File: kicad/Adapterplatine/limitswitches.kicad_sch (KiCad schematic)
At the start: 15 parts, among them X12 Conn_01x05_Pin, X13 Conn_01x05_Pin, X15 Conn_01x05_Pin, X16 Conn_01x05_Pin, X37 Conn_01x02_Pin, X39 Conn_01x02_Pin

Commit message: Leitungsverlegung Adapterplatine abgeschlossen
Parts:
- EndStopX1: Hersteller (none) -> Test
- R1, R2, R3: footprint Resistor_THT:R_Axial_DIN0207_L6.3mm_D2.5mm_P2.54mm_Vertical -> Resistor_THT:R_Axial_DIN0207_L6.3mm_D2.5mm_P10.16mm_Horizontal
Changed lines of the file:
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@@
 			)
 		)
-		(property "Footprint" "Resistor_THT:R_Axial_DIN0207_L6.3mm_D2.5mm_P2.54mm_Vertical"
+		(property "Footprint" "Resistor_THT:R_Axial_DIN0207_L6.3mm_D2.5mm_P10.16mm_Horizontal"
 			(at 46.482 73.66 90)
 			(hide yes)
@@
 		)
 		(property "Description" "Resistor"
+			(at 48.26 73.66 0)
+			(hide yes)
+			(show_name no)
+			(do_not_autoplace no)
+			(effects
+				(font
+					(size 1.27 1.27)
+				)
+			)
+		)
+		(property "Hersteller" ""
+			(at 48.26 73.66 0)
+			(hide yes)
+			(show_name no)
+			(do_not_autoplace no)
+			(effects
+				(font
+					(size 1.27 1.27)
+				)
+			)
+		)
+		(property "Herstellerbezeichnung" ""
+			(at 48.26 73.66 0)
+			(hide yes)
+			(show_name no)
+			(do_not_autoplace no)
+			(effects
+				(font
+					(size 1.27 1.27)
+				)
+			)
+		)
+		(property "Alternative" ""
 			(at 48.26 73.66 0)
 			(hide yes)
@@
 		)
 		(property "Description" "Generic connector, single row, 01x03, script generated (kicad-library-utils/schlib/autogen/connector/)"
+			(at 25.4 55.88 0)
+			(hide yes)
+			(show_name no)
+			(do_not_autoplace no)
+			(effects
+				(font
+					(size 1.27 1.27)
+				)
+			)
+		)
+		(property "Hersteller" "Test"
+			(at 25.4 55.88 0)
+			(hide yes)
+			(show_name no)
+			(do_not_autoplace no)
+			(effects
+				(font
+					(size 1.27 1.27)
+				)
+			)
+		)
+		(property "Herstellerbezeichnung" ""
+			(at 25.4 55.88 0)
+			(hide yes)
+			(show_name no)
+			(do_not_autoplace no)
+			(effects
+				(font
+					(size 1.27 1.27)
+				)
+			)
+		)
+		(property "Alternative" ""
 			(at 25.4 55.88 0)
 			(hide yes)
@@
 			)
 		)
-		(property "Footprint" "Resistor_THT:R_Axial_DIN0207_L6.3mm_D2.5mm_P2.54mm_Vertical"
+		(property "Footprint" "Resistor_THT:R_Axial_DIN0207_L6.3mm_D2.5mm_P10.16mm_Horizontal"
 			(at 18.542 73.66 90)
 			(hide yes)
@@
 		)
 		(property "Description" "Resistor"
+			(at 20.32 73.66 0)
+			(hide yes)
+			(show_name no)
+			(do_not_autoplace no)
+			(effects
+				(font
+					(size 1.27 1.27)
+				)
+			)
+		)
+		(property "Hersteller" ""
+			(at 20.32 73.66 0)
+			(hide yes)
+			(show_name no)
+			(do_not_autoplace no)
+			(effects
+				(font
+					(size 1.27 1.27)
+				)
+			)
+		)
+		(property "Herstellerbezeichnung" ""
+			(at 20.32 73.66 0)
+			(hide yes)
+			(show_name no)
+			(do_not_autoplace no)
+			(effects
+				(font
+					(size 1.27 1.27)
+				)
+			)
+		)
+		(property "Alternative" ""
 			(at 20.32 73.66 0)
 			(hide yes)
@@
 			)
 		)
-		(property "Footprint" "Resistor_THT:R_Axial_DIN0207_L6.3mm_D2.5mm_P2.54mm_Vertical"
+		(property "Footprint" "Resistor_THT:R_Axial_DIN0207_L6.3mm_D2.5mm_P10.16mm_Horizontal"
 			(at 76.962 73.66 90)
 			(hide yes)
@@
 			(at 78.74 73.66 0)
 			(hide yes)
+			(show_name no)
+			(do_not_autoplace no)
+			(effects
+				(font
+					(size 1.27 1.27)
+				)
+			)
+		)
+		(property "Hersteller" ""
+			(at 78.74 73.66 0)
+			(hide yes)
+			(show_name no)
+			(do_not_autoplace no)
+			(effects
+				(font
+					(size 1.27 1.27)
+				)
+			)
+		)
+		(property "Herstellerbezeichnung" ""
+			(at 78.74 73.66 0)
+			(hide yes)
+			(show_name no)
+			(do_not_autoplace no)
+			(effects
+				(font
+					(size 1.27 1.27)
+				)
+			)
+		)
+		(property "Alternative" ""
+			(at 78.74 73.66 0)
+			(hide yes)

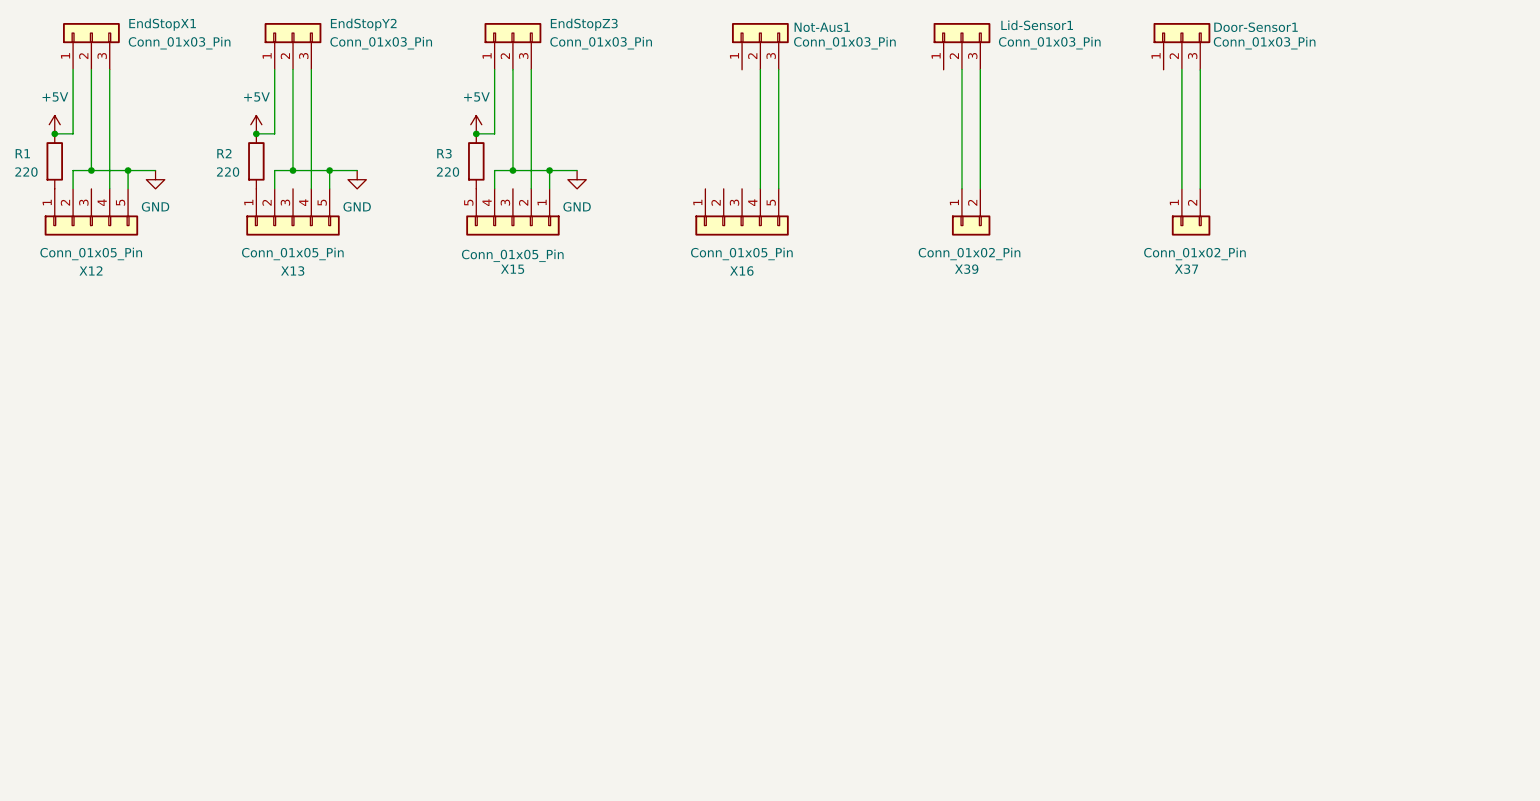
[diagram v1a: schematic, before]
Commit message: Einbau Vakuum Pumpe/ Einzeichnung Kraken benutze Pins
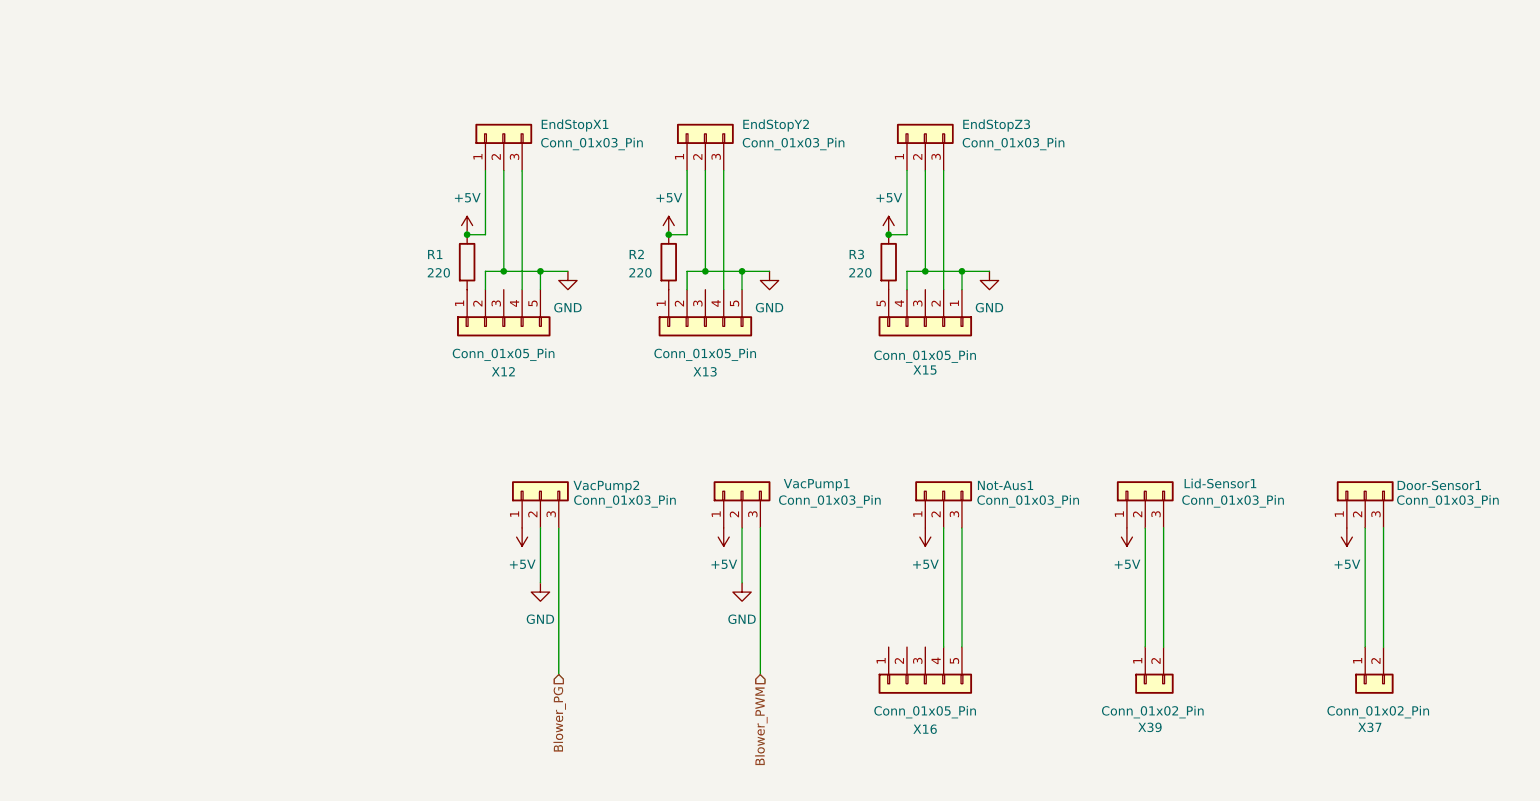
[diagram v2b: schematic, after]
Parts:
- added VacPump1, VacPump2: Conn_01x03_Pin, Connector_JST:JST_XH_B3B-XH-A_1x03_P2.50mm_Vertical, symbol Connector_Generic:Conn_01x03
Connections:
- net +5V: now also Door-Sensor1.1 (Pin_1), Lid-Sensor1.1 (Pin_1), Not-Aus1.1 (Pin_1), VacPump1.1 (Pin_1), VacPump2.1 (Pin_1)
- net GND: now also VacPump1.2 (Pin_2), VacPump2.2 (Pin_2)
- new net Blower_PG: VacPump2.3 (Pin_3)
- new net Blower_PWM: VacPump1.3 (Pin_3)
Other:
- moved on the sheet: Door-Sensor1, EndStopX1, EndStopY2, EndStopZ3, Lid-Sensor1, Not-Aus1, R1, R2, R3, X12, X13, X15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

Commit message: Abschlussbericht angefangen/ Adapterplatine ECR DCR
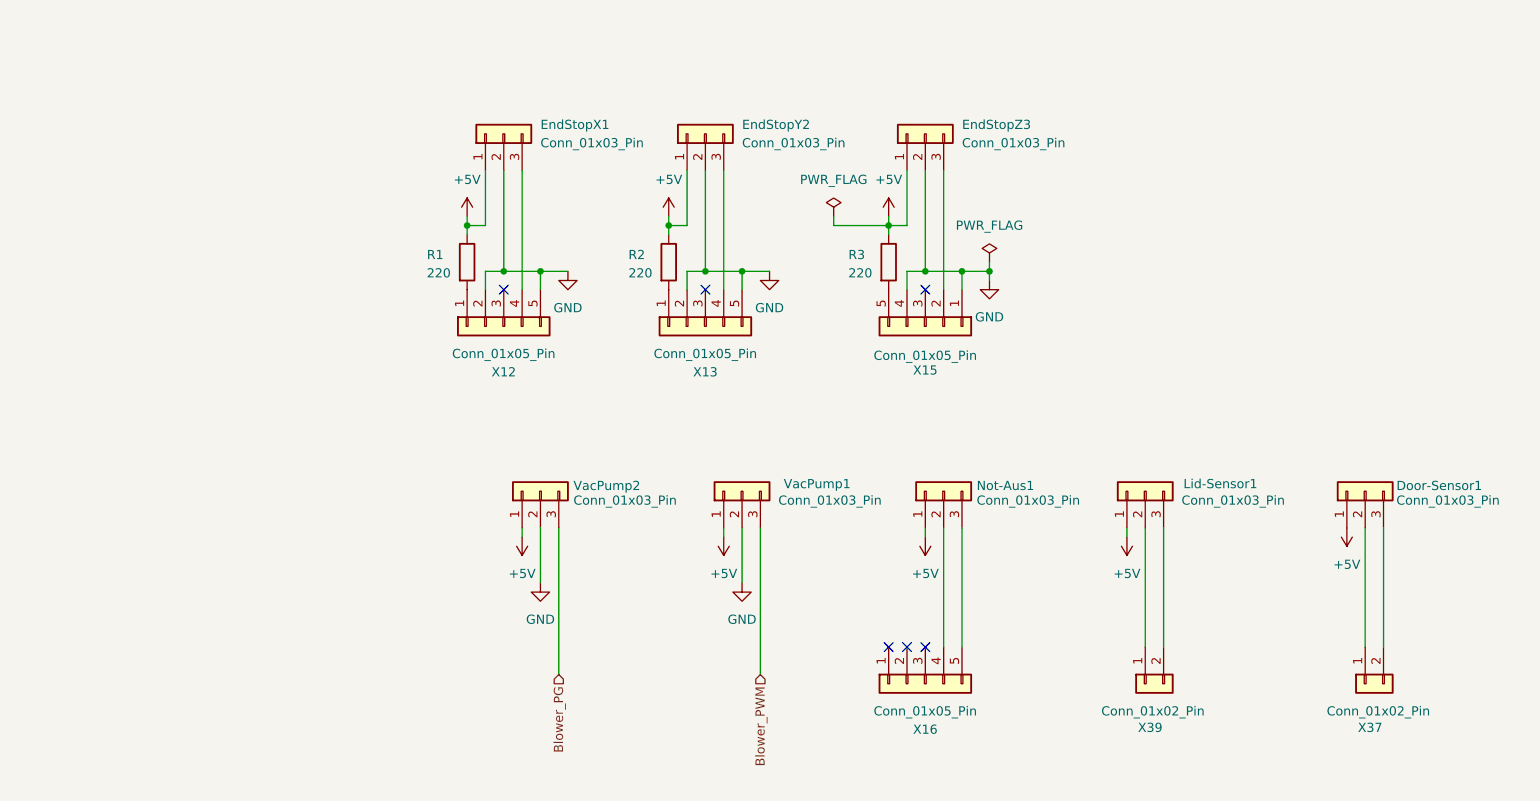
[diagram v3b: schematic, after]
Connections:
- no-connect marks 0 -> 6
